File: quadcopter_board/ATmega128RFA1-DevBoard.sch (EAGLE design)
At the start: 44 parts, among them J1 ISP, J2 ARDUINO_UNO_R3, J3 POWER_JACKPTH_LOCK, U1 ATMEGA128RFA1, U2 LM1117, Y1 16MHz

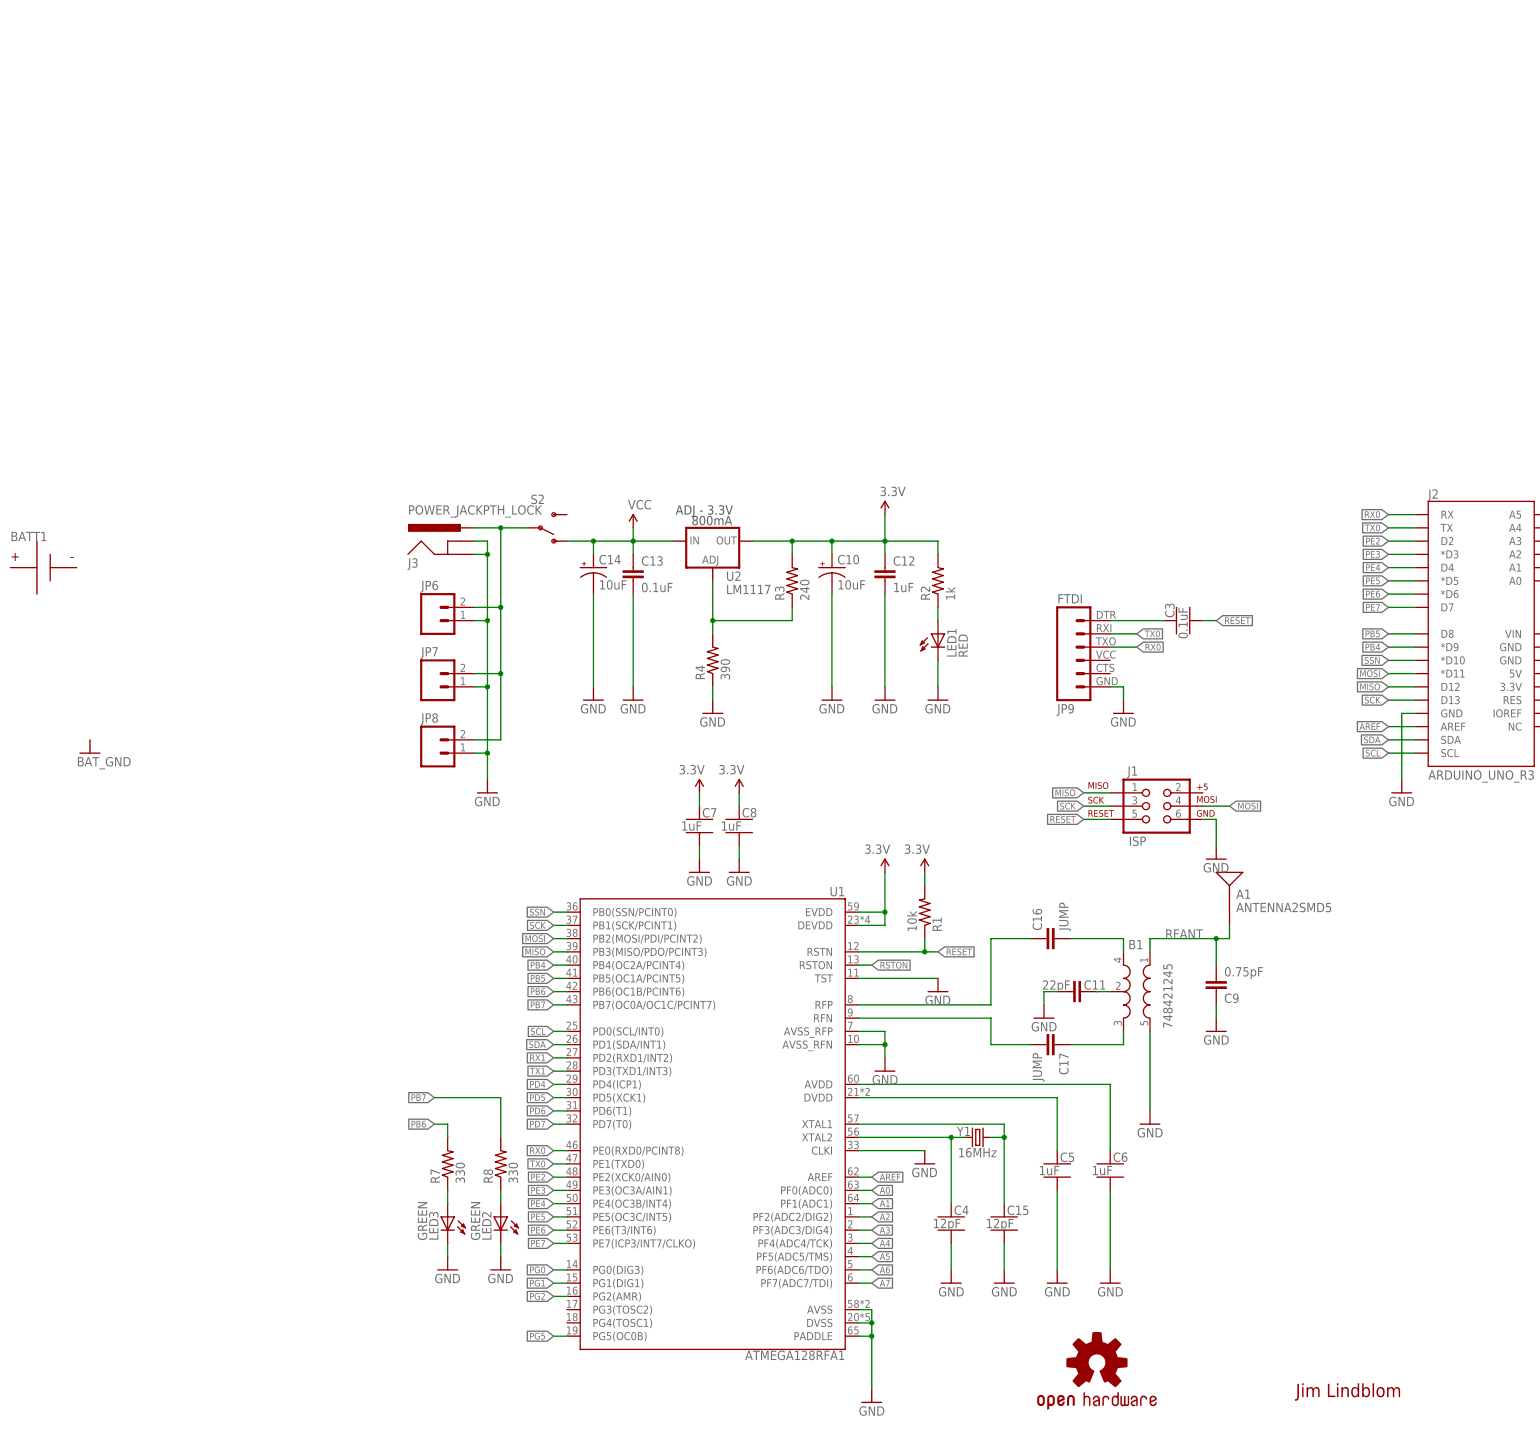
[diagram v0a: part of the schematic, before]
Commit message: added and wired imu
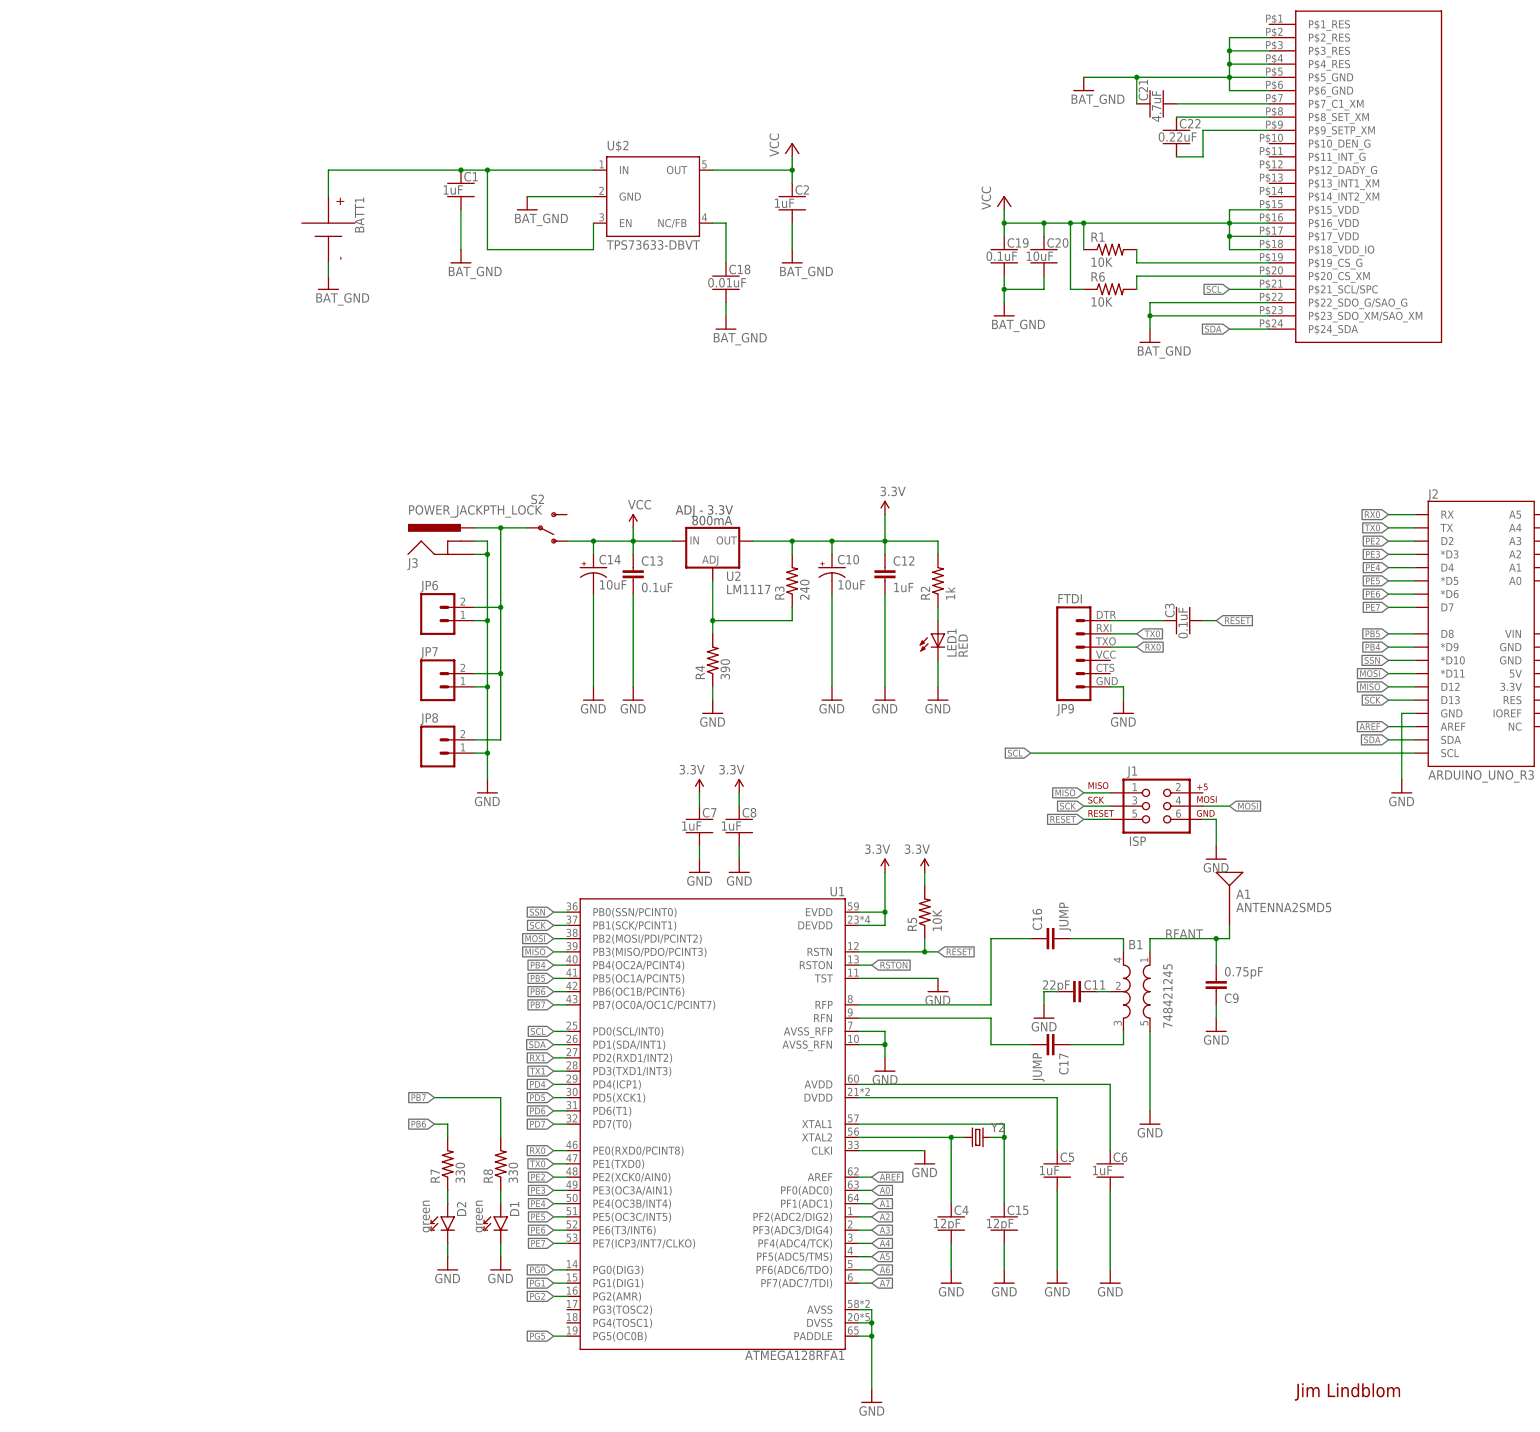
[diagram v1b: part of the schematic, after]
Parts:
- removed LED2, LED3: GREEN, SparkFun-LED:LED0603
- removed Y1: 16MHz, SparkFun-FreqCtrl:CRYSTAL5X3
- added C1, C2: 1uF, quadparts_prebuilt:CAPACITOR-NP_SMD-2012-0805_CERAMIC-1UF
- added C18: 0.01uF, quadparts_prebuilt:CAPACITOR-NP_SMD-2012-0805_CERAMIC-0.01UF
- added C19: 0.1uF, quadparts_prebuilt:CAPACITOR-NP_SMD-2012-0805_CERAMIC-0.1UF
- added C20: 10uF, quadparts_prebuilt:CAPACITOR-NP_SMD-2012-0805_CERAMIC-10UF
- added C21: 4.7uF, quadparts_prebuilt:CAPACITOR-NP_SMD-2012-0805_CERAMIC-4.7UF
- added C22: 0.22uF, quadparts_prebuilt:CAPACITOR-NP_SMD-2012-0805_CERAMIC-0.22UF
- added D1, D2: green, quadparts_prebuilt:DIODE-LED_SMD-2012-0805-GREEN
- added R5, R6: 10K, quadparts_prebuilt:RESISTOR_SMD-2012-0805-10K
- added U$2: TPS73633-DBVT, quadparts_prebuilt:TPS73633-DBVT
- added Y2: (no value), quadparts_prebuilt:CRYSTAL5X3
- R1: value 10k -> 10K; device SparkFun-Passives:RESISTOR0402-RES -> quadparts_prebuilt:RESISTOR_SMD-2012-0805-10K
- U$1: value OSHW-LOGOS -> IMU; device SparkFun-Aesthetics:OSHW-LOGOS -> quadparts:IMU
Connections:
- new net BAT_GND: BATT1.N, C1.2, C18.2, C19.2, C2.2, C20.2, C21.1, U$1.P$22_SDO_G/SAO_G, U$1.P$23_SDO_XM/SAO_XM, U$1.P$2_RES, U$1.P$3_RES, U$1.P$4_RES, U$1.P$5_GND, U$1.P$6_GND, U$2.GND
- new net N$1: BATT1.P, C1.1, U$2.EN, U$2.IN
- new net N$12: C22.1, U$1.P$8_SET_XM
- new net N$14: C22.2, U$1.P$9_SETP_XM
- new net N$15: R1.2, U$1.P$19_CS_G
- new net N$16: R6.2, U$1.P$20_CS_XM
- new net N$5: C18.1, U$2.NC/FB
- new net N$6: C21.2, U$1.P$7_C1_XM
- net 3.3V: now also R5.2; no longer R1.2
- net GND: now also D1.C, D2.C; no longer LED2.C, LED3.C
- net N$13: now also D1.A; no longer LED2.A
- net N$3: now also Y2.2; no longer Y1.2
- net N$4: now also Y2.1; no longer Y1.1
- net N$8: now also D2.A; no longer LED3.A
- net RESET: now also R5.1; no longer R1.1
- net SCL: now also U$1.P$21_SCL/SPC
- net SDA: now also U$1.P$24_SDA
- net VCC: now also C19.1, C2.1, C20.1, R1.1, R6.1, U$1.P$15_VDD, U$1.P$16_VDD, U$1.P$17_VDD, U$1.P$18_VDD_IO, U$2.OUT
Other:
- moved on the sheet: BATT1, R1

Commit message: added motor controller
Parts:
- removed J3: POWER_JACKPTH_LOCK, SparkFun-Connectors:POWER_JACKPTH_LOCK
- removed JP6: (no value), SparkFun-Connectors:M02JST-PTH-2
- removed JP7: (no value), SparkFun-Connectors:M021X02_NO_SILK
- removed JP8: (no value), SparkFun-Connectors:M023.5MM-NO_SILK
- added C23, C26, C29, C32: 1uf, Seeed-Capacitor-2016:CERAMIC-1UF-10V-10%-X5R(0402)
- added C24, C27, C30, C33: 100uf, Seeed-Capacitor-2016:TANTALUM-SMD-100UF-10V(AVX-B)
- added C25, C28, C31, C34: 1uf, Seeed-Capacitor-2016:CERAMIC-1UF-25V-10%-X7R(0603)
- added D3, D4, D5, D6: 28V-5A, Seeed-Diode-2016:SMD-DIODE-SCHOTTKY-28V-5A(DO-214AA)
- added J4: (no value), quadparts:MALE_HEADER_2POS-2X1-0.1IN
- added JP1: FTDI (Serial Only), SparkFun-Connectors:FTDI_BASICPTH
- added Q1, Q2, Q3, Q4: CJ2302, Seeed-Transistor-2016:SMD-MOSFET-N-CH-20V-2.1A-CJ2302(SOT-23)
- added R10, R12, R14, R16: 10K 1/10W, Seeed-Resistor-2016:SMD-RES-10K-5%-1/10W(0603)
- added R11, R13, R15, R9: 100R, Seeed-Resistor-2016:SMD-RES-100R-5%-1/10W(0603)
- added U$3: 0, quadparts:RESISTOR
- added U$4, U$5, U$6, U$7: MOTOR_PADS, Andranik-Lab4:MOTOR_PADS
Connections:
- removed net N$1: BATT1.P, C1.1, U$2.EN, U$2.IN
- new net N$17: BATT1.P, J4.1
- new net N$18: Q1.G, R10.2, R9.2
- new net N$19: C25.1, D3.+, Q1.D, U$4.V-
- new net N$21: Q2.G, R11.2, R12.2
- new net N$22: C28.1, D4.+, Q2.D, U$5.V-
- new net N$24: Q3.G, R13.2, R14.2
- new net N$25: C31.1, D5.+, Q3.D, U$6.V-
- new net N$27: Q4.G, R15.2, R16.2
- new net N$28: C34.1, D6.+, Q4.D, U$7.V-
- net 3.3V: now also C19.1, C2.1, C20.1, R1.1, R6.1, U$1.P$15_VDD, U$1.P$16_VDD, U$1.P$17_VDD, U$1.P$18_VDD_IO, U$2.OUT
- net BAT_GND: now also C23.1, C24.-, C26.1, C27.-, C29.1, C30.-, C32.1, C33.-, Q1.S, Q2.S, Q3.S, Q4.S, R10.1, R12.1, R14.1, R16.1, U$3.P$1; no longer C1.2, C18.2, C19.2, C2.2, C20.2, C21.1, U$1.P$22_SDO_G/SAO_G, U$1.P$23_SDO_XM/SAO_XM, U$1.P$2_RES, U$1.P$3_RES, U$1.P$4_RES, U$1.P$5_GND, U$1.P$6_GND, U$2.GND
- net GND: now also C1.2, C18.2, C19.2, C2.2, C20.2, C21.1, JP1.6, U$1.P$22_SDO_G/SAO_G, U$1.P$23_SDO_XM/SAO_XM, U$1.P$2_RES, U$1.P$3_RES, U$1.P$4_RES, U$1.P$5_GND, U$1.P$6_GND, U$2.GND, U$3.P$2; no longer J3.GND, J3.GNDBREAK, JP6.1, JP7.1, JP8.1
- net N$9: no longer J3.PWR, JP6.2, JP7.2, JP8.2
- net PB5: now also R9.1
- net PE3: now also R13.1
- net PE4: now also R15.1
- net PE5: now also R11.1
- net RX1: now also JP1.2
- net TX1: now also JP1.3
- net VCC: now also C1.1, C24.+, C25.2, C27.+, C28.2, C30.+, C31.2, C33.+, C34.2, D3.-, D4.-, D5.-, D6.-, J4.2, U$2.EN, U$2.IN, U$4.V+, U$5.V+, U$6.V+, U$7.V+; no longer C19.1, C2.1, C20.1, R1.1, R6.1, U$1.P$15_VDD, U$1.P$16_VDD, U$1.P$17_VDD, U$1.P$18_VDD_IO, U$2.OUT
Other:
- moved on the sheet: BATT1

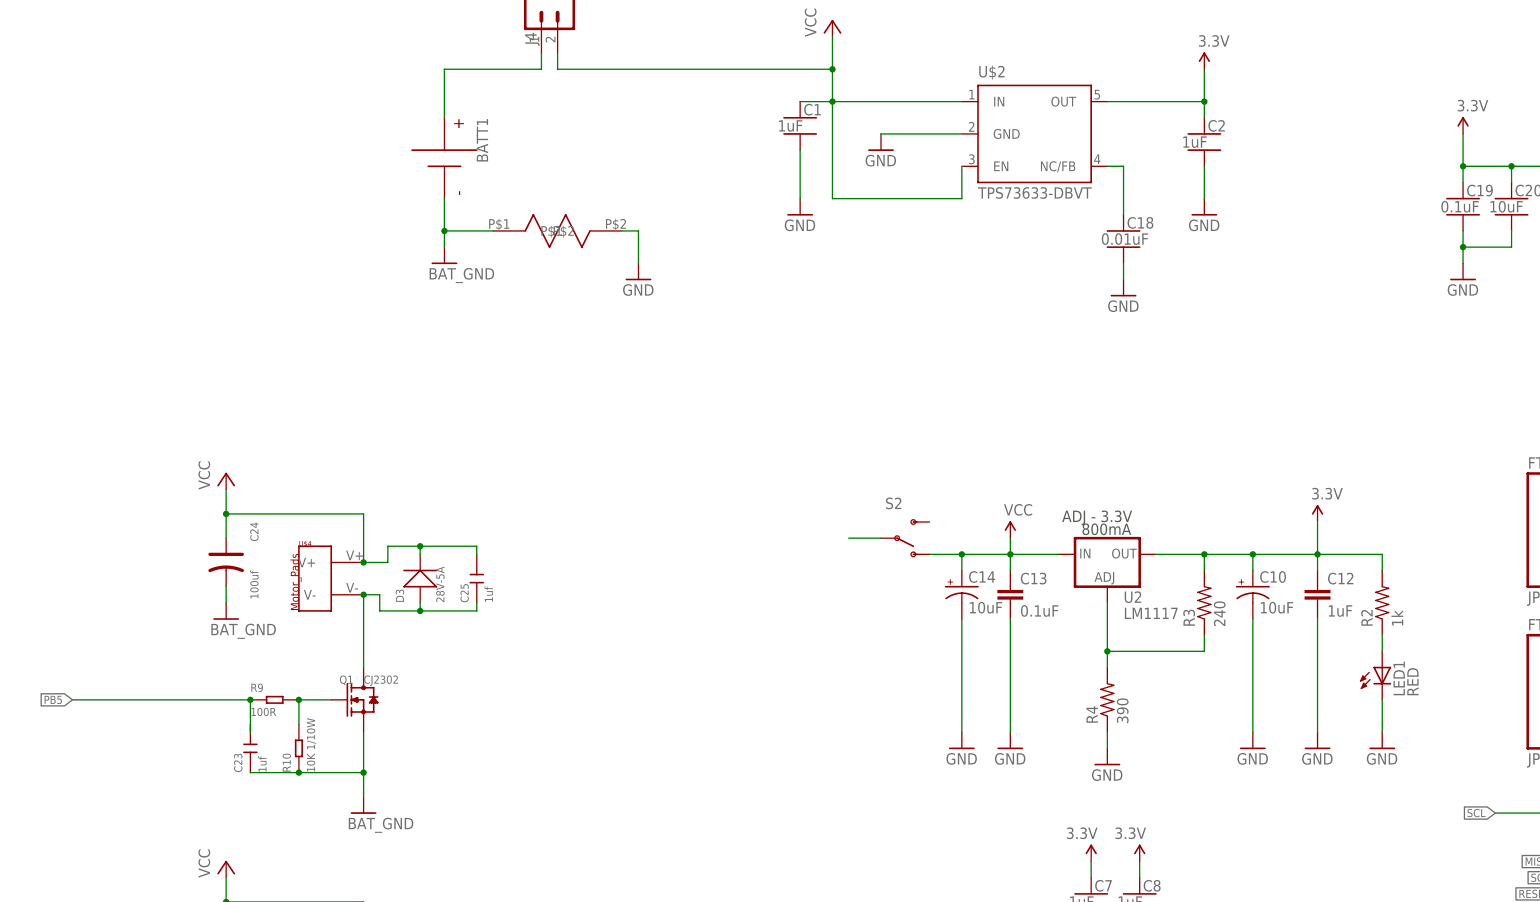
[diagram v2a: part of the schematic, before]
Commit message: added bigger cap to power supply
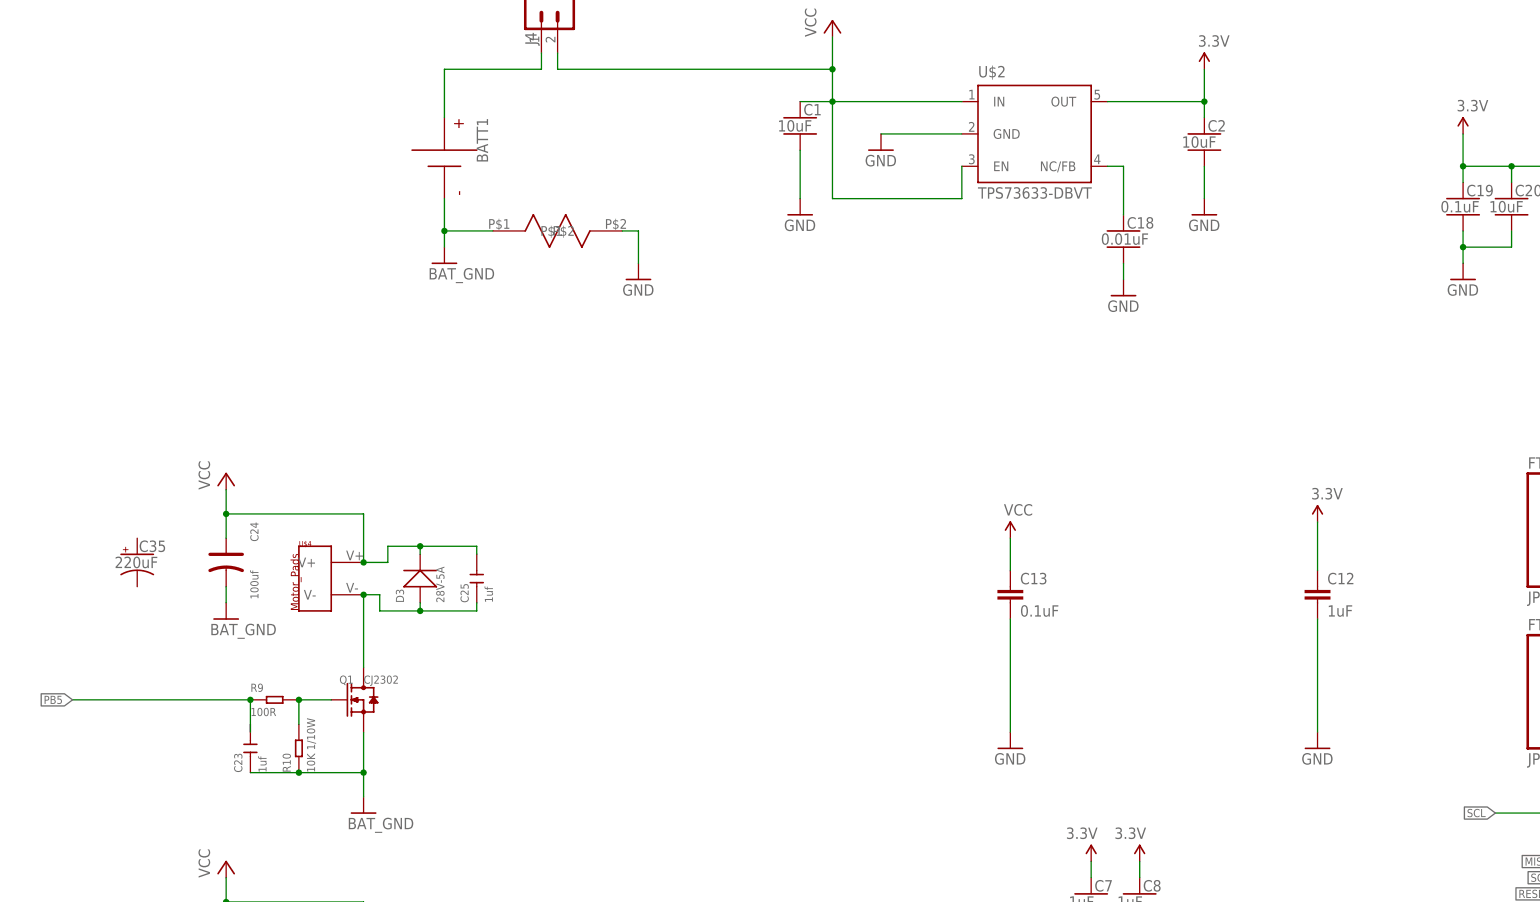
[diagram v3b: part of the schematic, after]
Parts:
- removed C10, C14: 10uF, SparkFun-Passives:CAP_POL1206
- removed LED1: RED, SparkFun-LED:LED0603
- removed R2: 1k, SparkFun-Passives:RESISTOR0402-RES
- removed R3: 240, SparkFun:RESISTOR0402-RES
- removed R4: 390, SparkFun:RESISTOR0402-RES
- removed S2: (no value), SparkFun:SWITCH-SPST-SMD-A
- removed U2: LM1117, SparkFun:V_REG_317SMD
- added C35: 220uF, quadparts_prebuilt:CAPACITOR-POL_SMD-7043-D_TANTALUM-220UF
- C1, C2: value 1uF -> 10uF; device quadparts_prebuilt:CAPACITOR-NP_SMD-2012-0805_CERAMIC-1UF -> quadparts_prebuilt:CAPACITOR-NP_SMD-2012-0805_CERAMIC-10UF
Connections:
- removed net FB: R3.1, R4.2, U2.ADJ
- removed net N$2: LED1.A, R2.1
- removed net N$9: S2.P
- net 3.3V: no longer C10.+, R2.2, R3.2, U2.OUT
- net GND: no longer C10.-, C14.-, LED1.C, R4.1
- net VCC: no longer C14.+, S2.O, U2.IN
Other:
- note removed: "800mA"
- note removed: "ADJ - 3.3V"

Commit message: added tags
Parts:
- removed C12: 1uF, SparkFun-Passives:CAP0402-CAP
- removed C13: 0.1uF, SparkFun-Passives:CAP0402-CAP
- removed C35: 220uF, quadparts_prebuilt:CAPACITOR-POL_SMD-7043-D_TANTALUM-220UF
- removed J2: ARDUINO_UNO_R3, SparkFun-Boards:ARDUINO_UNO_R3
- removed S1: SWITCH-MOMENTARY-2SMD, SparkFun-Electromechanical:SWITCH-MOMENTARY-2SMD
- added C10: 0.75pF, quadparts_prebuilt:CAPACITOR-NP_SMD-2012-0805_CERAMIC-0.75PF
- added C14: 22pF, quadparts_prebuilt:CAPACITOR-NP_SMD-2012-0805_CERAMIC-22PF
- C16: value JUMP -> 1uF; device SparkFun:CAP0402-CAP -> quadparts_prebuilt:CAPACITOR-NP_SMD-2012-0805_CERAMIC-1UF
- C17: value JUMP -> 0.1uF; device SparkFun:CAP0402-CAP -> quadparts_prebuilt:CAPACITOR-NP_SMD-2012-0805_CERAMIC-0.1UF
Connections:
- removed net N$10: B1.OUT1, C16.2
- removed net N$11: B1.OUT2, C17.1
- net 3.3V: now also C16.1; no longer C12.1, J2.3.3V, J2.5V
- net A0: no longer J2.A0
- net A1: no longer J2.A1
- net A2: no longer J2.A2
- net A3: no longer J2.A3
- net A4: no longer J2.A4
- net A5: no longer J2.A5
- net AREF: no longer J2.AREF
- net GND: now also C16.2, C17.2; no longer C12.2, C13.2, J2.GND@0, J2.GND@1, J2.GND@2, S1.2
- net MISO: no longer J2.D12
- net MOSI: no longer J2.*D11
- net PB4: no longer J2.*D9
- net PB5: no longer J2.D8
- net PE2: no longer J2.D2
- net PE3: no longer J2.*D3
- net PE4: now also C32.2; no longer J2.D4
- net PE5: no longer J2.*D5
- net PE6: no longer J2.*D6
- net PE7: no longer J2.D7
- net RESET: no longer J2.RES, S1.1
- net RFN: now also B1.OUT2; no longer C17.2
- net RFP: now also B1.OUT1; no longer C16.1
- net RX0: no longer J2.RX
- net SCK: no longer J2.D13
- net SCL: no longer J2.SCL
- net SDA: no longer J2.SDA
- net SSN: no longer J2.*D10
- net TX0: no longer J2.TX
- net VCC: now also C17.1; no longer C13.1, J2.VIN
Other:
- moved on the sheet: C3, C32, C33, C34, C7, C8, D1, D2, D6, J1, JP1, JP9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
